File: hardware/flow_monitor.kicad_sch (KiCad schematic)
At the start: 80 parts, among them J1 Conn_01x04_Pin, J2 USB_C_Receptacle_USB2.0_16P, J3 Conn_01x02_Socket, J4 Conn_01x02_Socket, J5 Conn_01x02_Socket, Q1 2N7002, Q2 IRLML6402, Q3 BC807, Q4 BC817, Q6 2N7002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

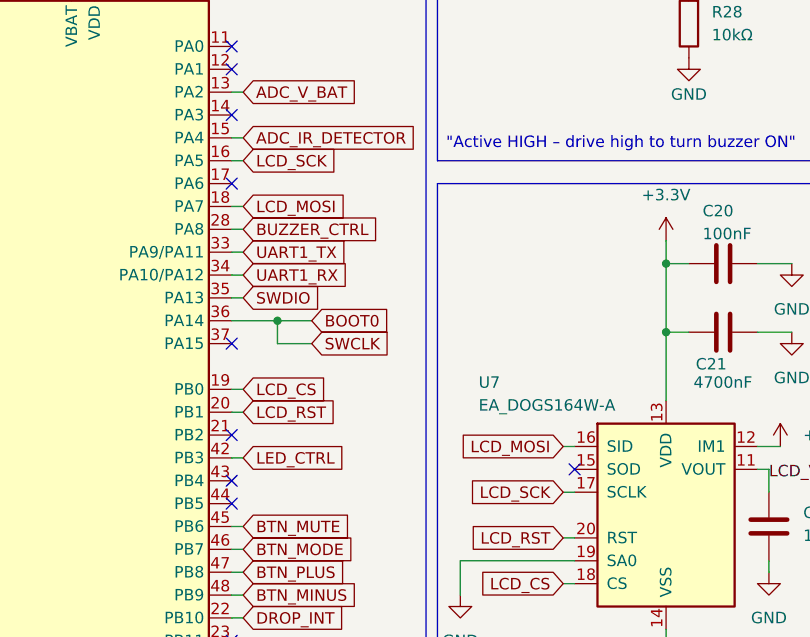
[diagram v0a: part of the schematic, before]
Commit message: Added MISO routing to LCD Screen
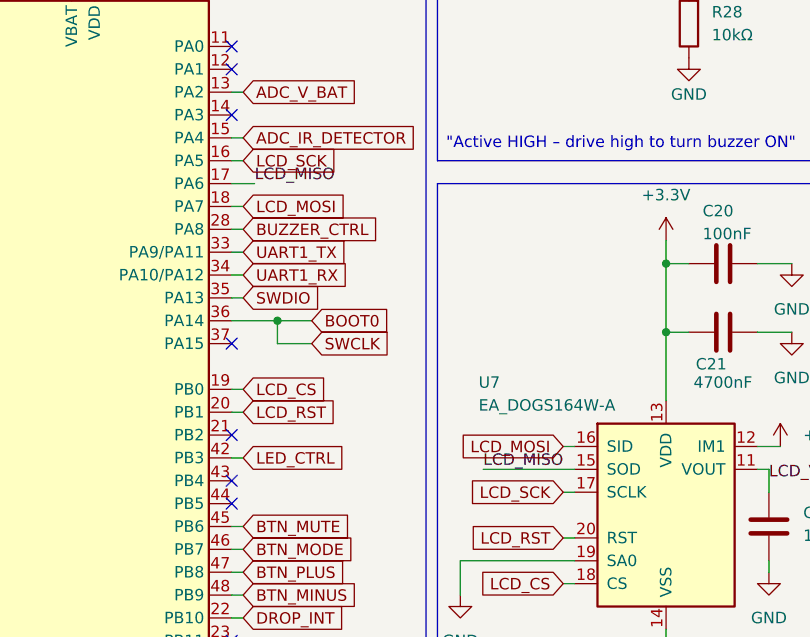
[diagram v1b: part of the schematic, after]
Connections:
- net LCD_MISO: now reaches U7.15 (SOD)
- net LCD_MISO: now also U6.17 (PA6)
- no-connect marks 46 -> 44
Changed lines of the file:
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@@
-	)
-	(no_connect
-		(at 300.99 92.71)
 	)
 	(no_connect
@@
 	)
 	(no_connect
-		(at 339.09 124.46)
-	)
-	(no_connect
 		(at 297.18 195.58)
 	)
@@
 	(wire
 		(pts
+			(xy 303.53 92.71) (xy 300.99 92.71)
+		)
+		(stroke
+			(width 0)
+			(type default)
+		)
+	)
+	(wire
+		(pts
 			(xy 241.3 123.19) (xy 252.73 123.19)
 		)
@@
 		(pts
 			(xy 360.68 124.46) (xy 359.41 124.46)
+		)
+		(stroke
+			(width 0)
+			(type default)
+		)
+	)
+	(wire
+		(pts
+			(xy 328.93 124.46) (xy 339.09 124.46)
 		)
 		(stroke
@@
 		)
 	)
+	(label "LCD_MISO"
+		(at 328.93 124.46 0)
+		(effects
+			(font
+				(size 1.27 1.27)
+			)
+			(justify left bottom)
+		)
+	)
 	(label "LCD_VOUT"
 		(at 360.68 125.73 0)
 		(effects
 			(font
+				(size 1.27 1.27)
+			)
+			(justify left bottom)
+		)
+	)
+	(label "LCD_MISO"
+		(at 303.53 92.71 0)
+		(effects
+			(font

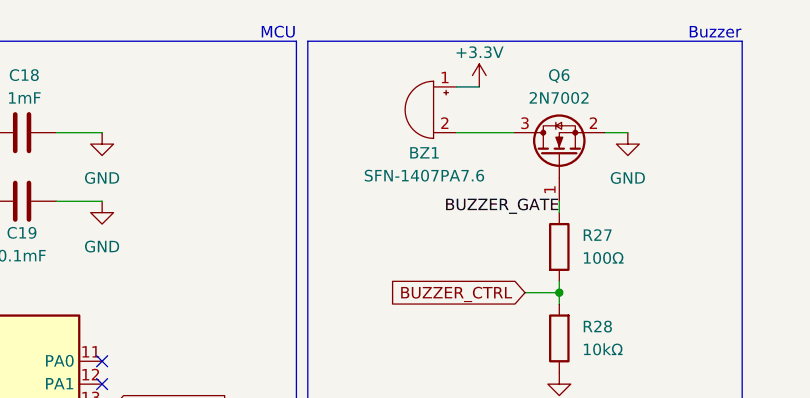
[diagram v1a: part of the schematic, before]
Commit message: Added Bleed Resistor to buzzer schematic
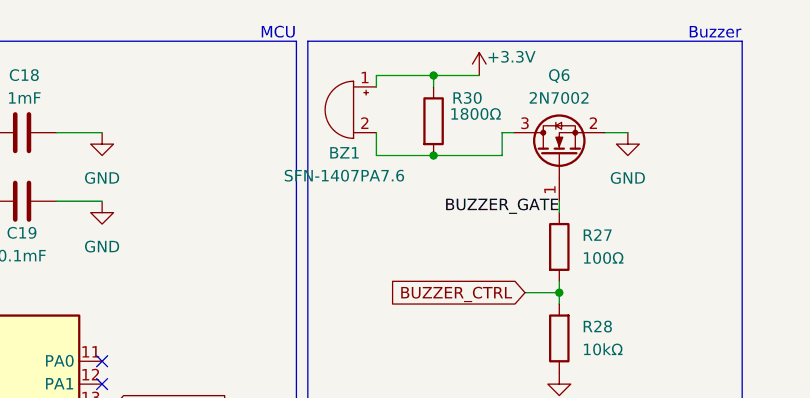
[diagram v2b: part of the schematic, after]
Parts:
- added R30: 1800Ω, symbol Device:R
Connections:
- net +3.3V: now also R30.1
- net at BZ1.2 (-), Q6.3 (D): now also R30.2
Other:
- moved on the sheet: BZ1

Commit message: small changes
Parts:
- removed R15: 10kΩ, Resistor_SMD:R_0603_1608Metric, symbol Device:R
- added R31: 1MΩ, Resistor_SMD:R_0603_1608Metric, symbol Device:R
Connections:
- net GND: now also R31.2
- net VREF = 1.65V: now also R31.1

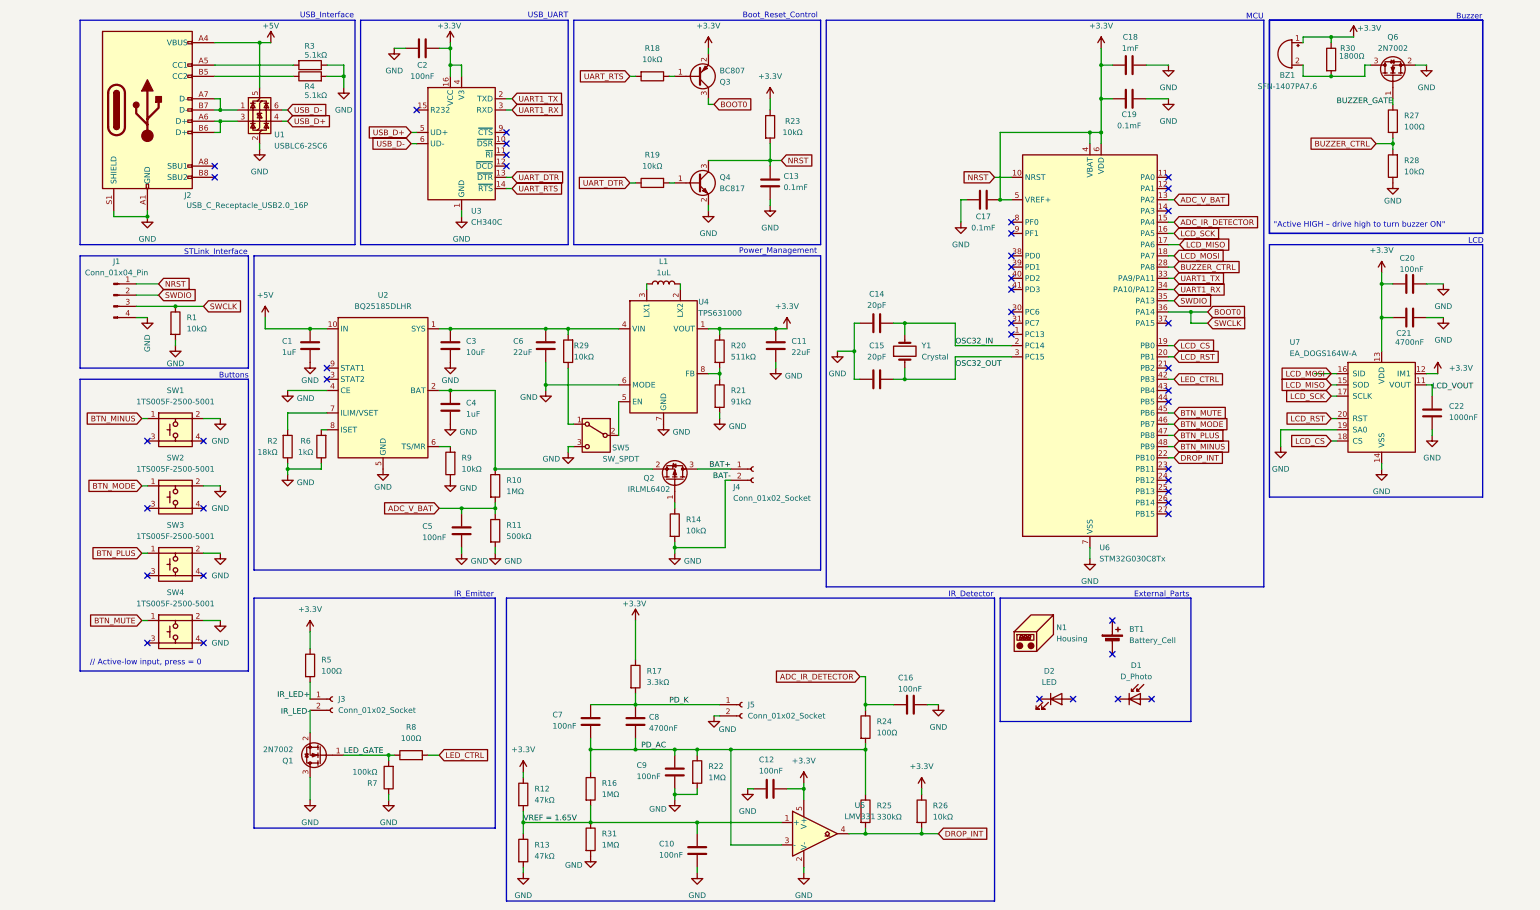
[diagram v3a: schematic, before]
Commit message: remove comparator circuit from drop detector
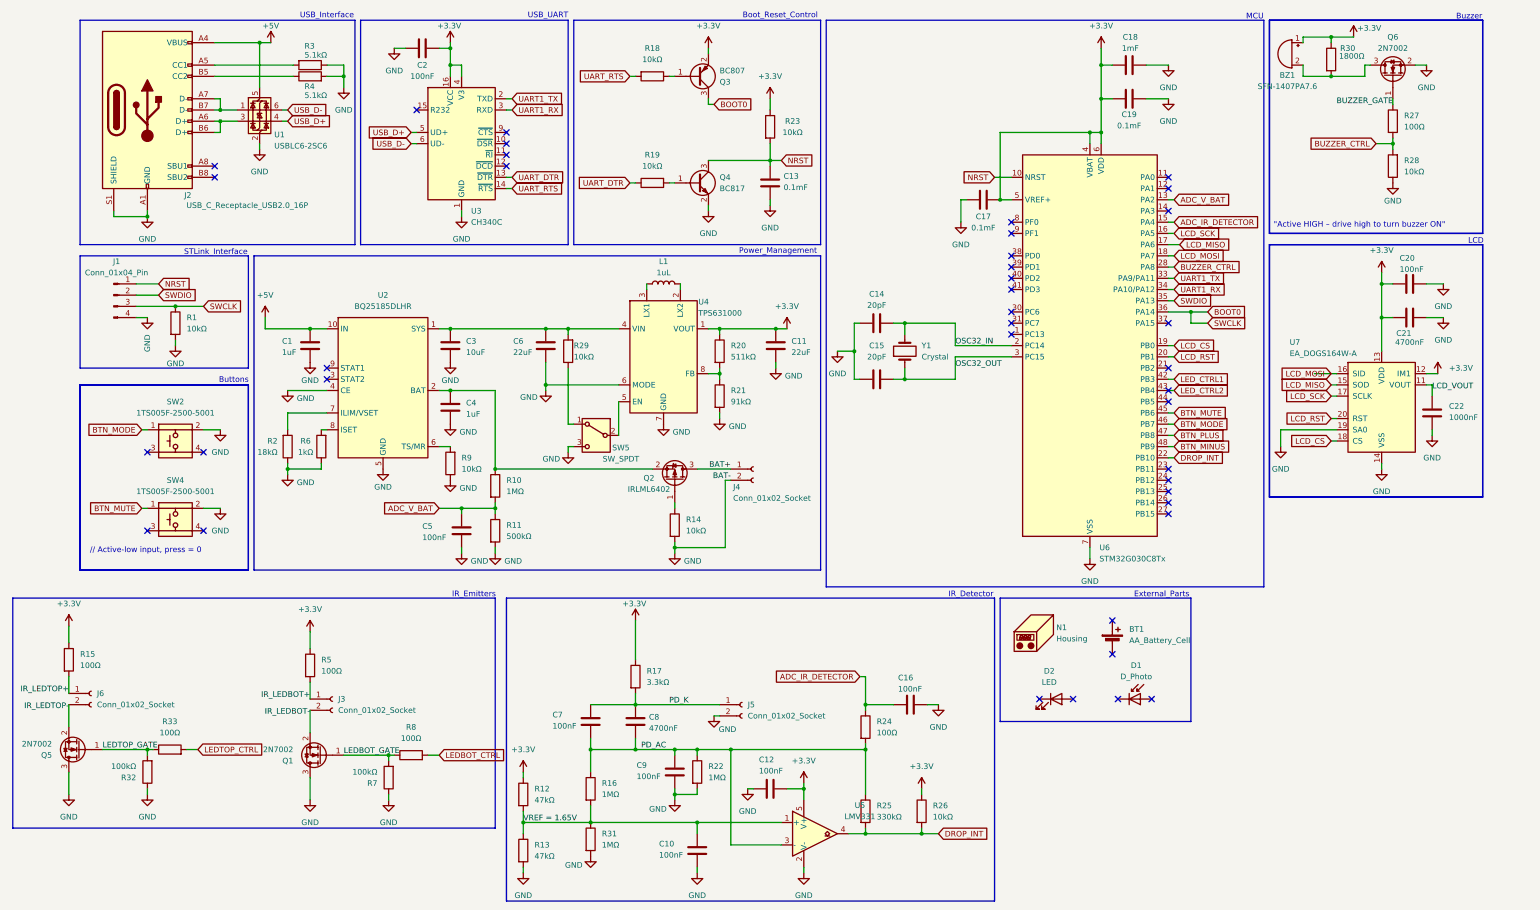
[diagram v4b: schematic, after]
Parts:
- removed SW1, SW3: 1TS005F-2500-5001, IV_Flow_Monitor_Footprints:SW_HYP_1TS005F-2500-5001, symbol IV_Flow_Monitor_Symbols:SW_HYP_1TS005F-2500-5001
- added J6: Conn_01x02_Socket, Connector_Wire:SolderWire-0.1sqmm_1x02_P3.6mm_D0.4mm_OD1mm_Relief, symbol Connector:Conn_01x02_Socket
- added Q5: 2N7002, Package_TO_SOT_SMD:SOT-23, symbol Transistor_FET:2N7002
- added R15, R33: 100Ω, Resistor_SMD:R_0603_1608Metric, symbol Device:R
- added R32: 100kΩ, Resistor_SMD:R_0603_1608Metric, symbol Device:R
- BT1: value Battery_Cell -> AA_Battery_Cell
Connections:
- net +3.3V: now also R15.1
- net GND: now also Q5.3 (D), R32.1
- net LED_CTRL2: now reaches U6.43 (PB4)
- net IR_LED+ renamed IR_LEDBOT+
- net IR_LED- renamed IR_LEDBOT-
- net LED_CTRL renamed LEDBOT_CTRL
- net LEDBOT_CTRL: no longer U6.42 (PB3)
- net LED_GATE renamed LEDBOT_GATE
- new net IR_LEDTOP+: J6.1 (Pin_1), R15.2
- new net IR_LEDTOP-: J6.2 (Pin_2), Q5.2 (S)
- new net LEDTOP_CTRL: R33.2
- new net LEDTOP_GATE: Q5.1 (G), R32.2, R33.1
- new net LED_CTRL1: U6.42 (PB3)
- no-connect marks 44 -> 40
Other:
- note added: "IR_Emitters"
- note removed: "IR_Emitter"
- moved on the sheet: SW2, SW4

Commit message: add bottom/top photodiode circuit
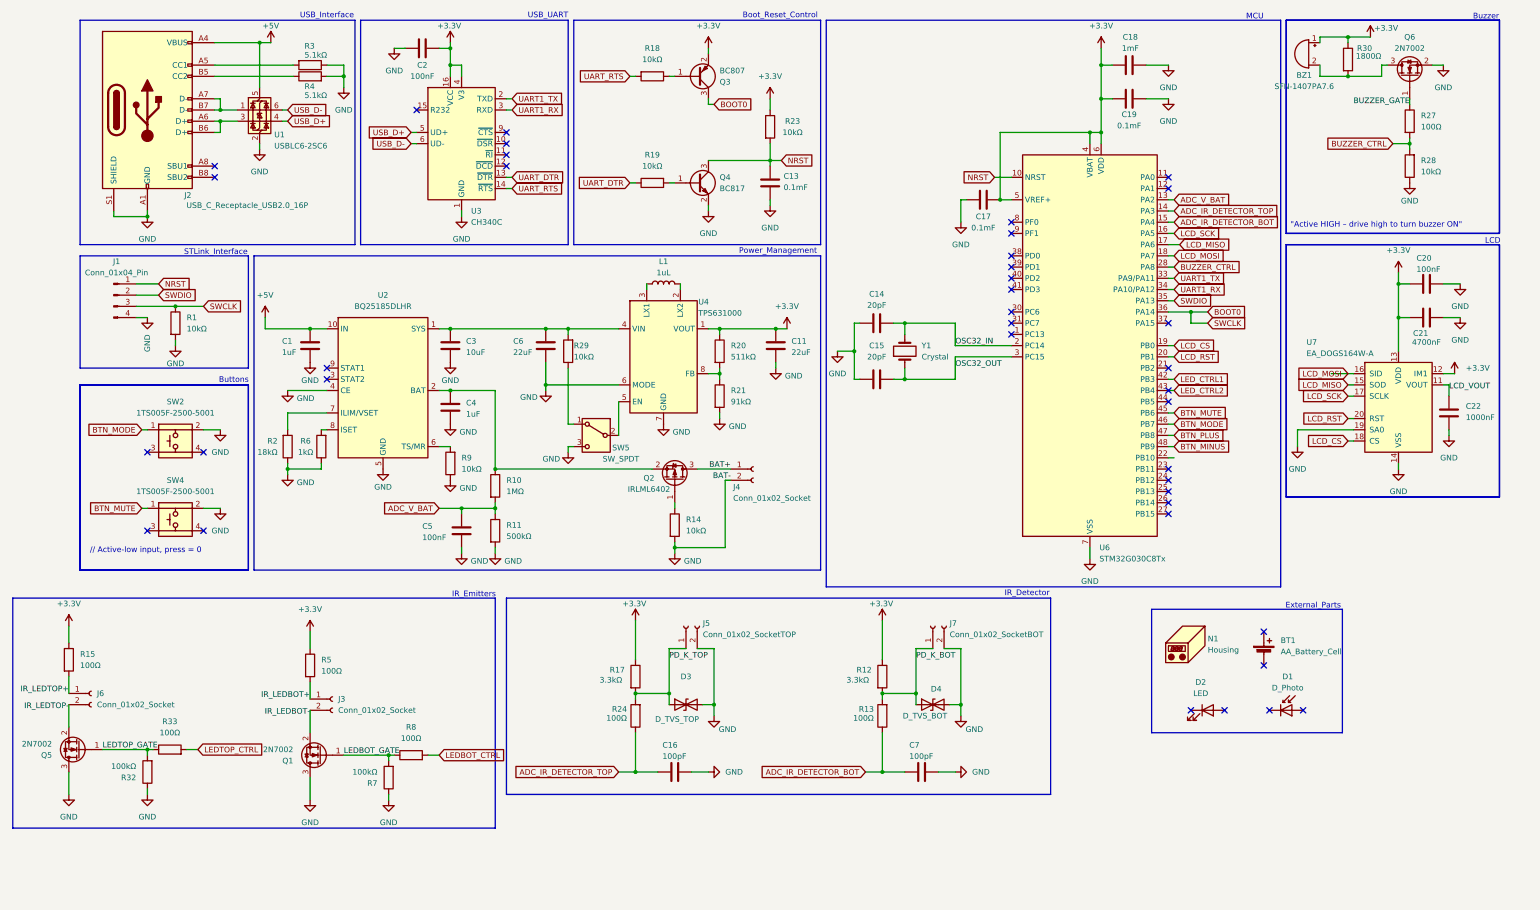
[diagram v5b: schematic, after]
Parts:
- removed C10, C12, C9: 100nF, Capacitor_SMD:C_0603_1608Metric, symbol Device:C
- removed C8: 4700nF, Capacitor_SMD:C_0805_2012Metric, symbol Device:C
- removed R16, R22, R31: 1MΩ, Resistor_SMD:R_0603_1608Metric, symbol Device:R
- removed R25: 330kΩ, Resistor_SMD:R_0603_1608Metric, symbol Device:R
- removed R26: 10kΩ, Resistor_SMD:R_0603_1608Metric, symbol Device:R
- removed U5: LMV331, Package_TO_SOT_SMD:SOT-23-5, symbol Comparator:LMV331
- added D3: D_TVS_TOP, symbol Device:D_TVS
- added D4: D_TVS_BOT, symbol Device:D_TVS
- added J7: Conn_01x02_SocketBOT, Connector_Wire:SolderWire-0.1sqmm_1x02_P3.6mm_D0.4mm_OD1mm_Relief, symbol Connector:Conn_01x02_Socket
- C16: value 100nF -> 100pF
- C7: value 100nF -> 100pF; Mfr. No. CL10B104KA8NNNC -> (none)
- J5: value Conn_01x02_Socket -> Conn_01x02_SocketTOP
- R12: value 47kΩ -> 3.3kΩ
- R13: value 47kΩ -> 100Ω
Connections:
- net GND: now also C7.1, D3.2 (A2), D4.2 (A2), J7.2 (Pin_2); no longer R13.2
- net ADC_IR_DETECTOR_TOP: now reaches U6.14 (PA3)
- net ADC_IR_DETECTOR_TOP: now also C16.2, R24.1
- removed net ADC_IR_DETECTOR: C16.2, R24.1, U6.15 (PA4)
- net DROP_INT: no longer names the net of U6.22 (PB10)
- net PD_AC renamed PD_K_TOP
- net PD_K_TOP: now also J5.1 (Pin_1), R17.2, D3.1 (A1); no longer C7.1
- removed net PD_K: C7.2, J5.1 (Pin_1), R17.2
- net VREF = 1.65V renamed ADC_IR_DETECTOR_BOT
- net ADC_IR_DETECTOR_BOT: now also C7.2, U6.15 (PA4); no longer R12.2
- new net PD_K_BOT: D4.1 (A1), J7.1 (Pin_1), R12.2, R13.2
- no-connect marks 40 -> 39
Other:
- moved on the sheet: BT1, BZ1, C16, C20, C21, C22, D1, D2, J5, N1, Q6, R24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
